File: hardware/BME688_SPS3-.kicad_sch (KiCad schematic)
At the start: 6 parts, among them U401 BME688, U402 USBLC6-2P6

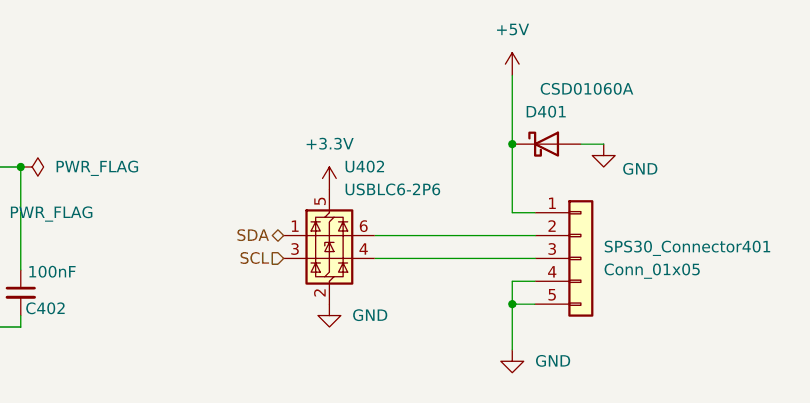
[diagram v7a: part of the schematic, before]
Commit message: added QON pushbutton
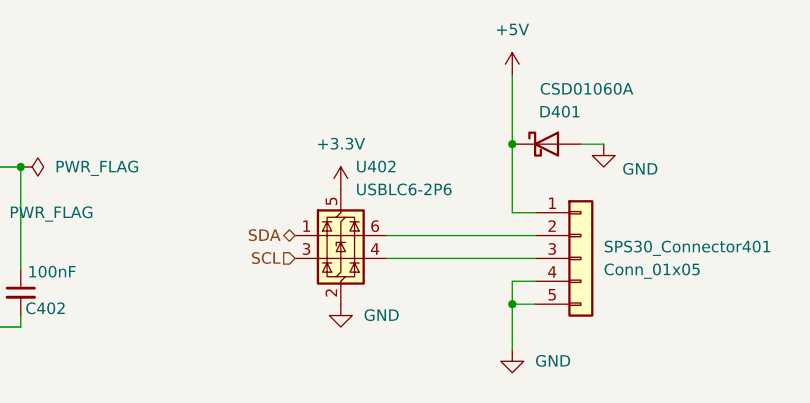
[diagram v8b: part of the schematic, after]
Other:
- moved on the sheet: U402
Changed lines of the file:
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@@
 	(wire
 		(pts
-			(xy 175.26 114.3) (xy 193.04 114.3)
+			(xy 176.53 114.3) (xy 193.04 114.3)
 		)
 		(stroke
@@
 	(wire
 		(pts
-			(xy 175.26 111.76) (xy 193.04 111.76)
+			(xy 176.53 111.76) (xy 193.04 111.76)
 		)
 		(stroke
@@
 	(hierarchical_label "SDA"
 		(shape bidirectional)
-		(at 165.1 111.76 180)
+		(at 166.37 111.76 180)
 		(effects
 			(font
@@
 	(hierarchical_label "SCL"
 		(shape input)
-		(at 165.1 114.3 180)
+		(at 166.37 114.3 180)
 		(effects
 			(font
@@
 	(symbol
 		(lib_id "Power_Protection:USBLC6-2P6")
-		(at 170.18 111.76 0)
+		(at 171.45 111.76 0)
 		(unit 1)
 		(exclude_from_sim no)
@@
 		(fields_autoplaced yes)
 		(property "Reference" "U402"
-			(at 171.8311 104.14 0)
+			(at 173.1011 104.14 0)
 			(effects
 				(font
@@
 		)
 		(property "Value" "USBLC6-2P6"
-			(at 171.8311 106.68 0)
+			(at 173.1011 106.68 0)
 			(effects
 				(font
@@
 		)
 		(property "Footprint" "Package_TO_SOT_SMD:SOT-666"
-			(at 171.196 118.491 0)
+			(at 172.466 118.491 0)
 			(effects
 				(font
@@
 		)
 		(property "Datasheet" "https://www.st.com/resource/en/datasheet/usblc6-2.pdf"
-			(at 171.196 120.396 0)
+			(at 172.466 120.396 0)
 			(effects
 				(font
@@
 		)
 		(property "Description" "Very low capacitance ESD protection diode, 2 data-line, SOT-666"
-			(at 170.18 111.76 0)
+			(at 171.45 111.76 0)
 			(effects
 				(font
@@
 	(symbol
 		(lib_id "power:+3.3V")
-		(at 170.18 106.68 0)
+		(at 171.45 106.68 0)
 		(unit 1)
 		(exclude_from_sim no)
@@
 		(fields_autoplaced yes)
 		(property "Reference" "#PWR0403"
-			(at 170.18 110.49 0)
+			(at 171.45 110.49 0)
 			(effects
 				(font
@@
 		)
 		(property "Value" "+3.3V"
-			(at 170.18 101.6 0)
+			(at 171.45 101.6 0)
 			(effects
 				(font
@@
 		)
 		(property "Footprint" ""
-			(at 170.18 106.68 0)
+			(at 171.45 106.68 0)
 			(effects
 				(font
@@
 		)
 		(property "Datasheet" ""
-			(at 170.18 106.68 0)
+			(at 171.45 106.68 0)
 			(effects
 				(font
@@
 		)
 		(property "Description" "Power symbol creates a global label with name \"+3.3V\""
-			(at 170.18 106.68 0)
+			(at 171.45 106.68 0)
 			(effects
 				(font
@@
 		(dnp no)
 		(property "Reference" "D401"
-			(at 196.596 98.044 0)
+			(at 198.12 98.044 0)
 			(effects
 				(font
@@
 	(symbol
 		(lib_id "power:GND")
-		(at 170.18 119.38 0)
+		(at 171.45 119.38 0)
 		(unit 1)
 		(exclude_from_sim no)
@@
 		(fields_autoplaced yes)
 		(property "Reference" "#PWR0405"
-			(at 170.18 125.73 0)
+			(at 171.45 125.73 0)
 			(effects
 				(font
@@
 		)
 		(property "Value" "GND"
-			(at 172.72 120.6499 0)
+			(at 173.99 120.6499 0)
 			(effects
 				(font
@@
 		)
 		(property "Footprint" ""
-			(at 170.18 119.38 0)
+			(at 171.45 119.38 0)
 			(effects
 				(font
@@
 		)
 		(property "Datasheet" ""
-			(at 170.18 119.38 0)
+			(at 171.45 119.38 0)
 			(effects
 				(font
@@
 		)
 		(property "Description" "Power symbol creates a global label with name \"GND\" , ground"
-			(at 170.18 119.38 0)
-			(effects
-				(font
+			(at 171.45 119.38 0)
+			(effects
+				(font
